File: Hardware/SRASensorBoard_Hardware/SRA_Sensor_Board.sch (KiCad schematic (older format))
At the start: 16 parts

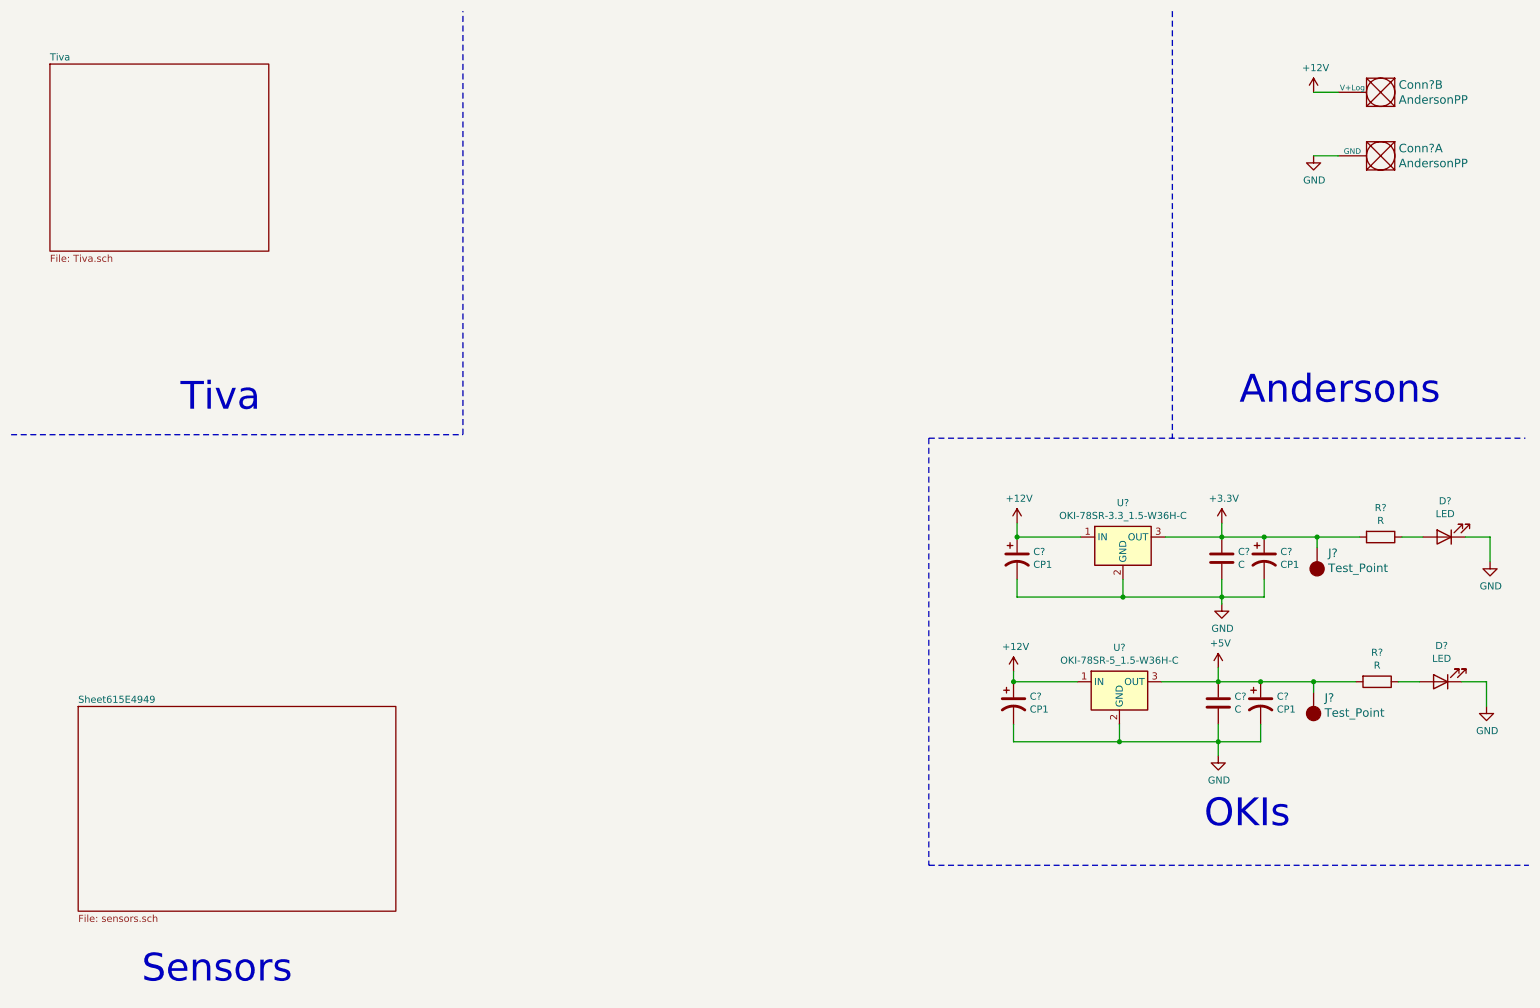
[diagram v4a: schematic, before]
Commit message: Added NH3 sensor and MOSFETS, fixed tiva pins
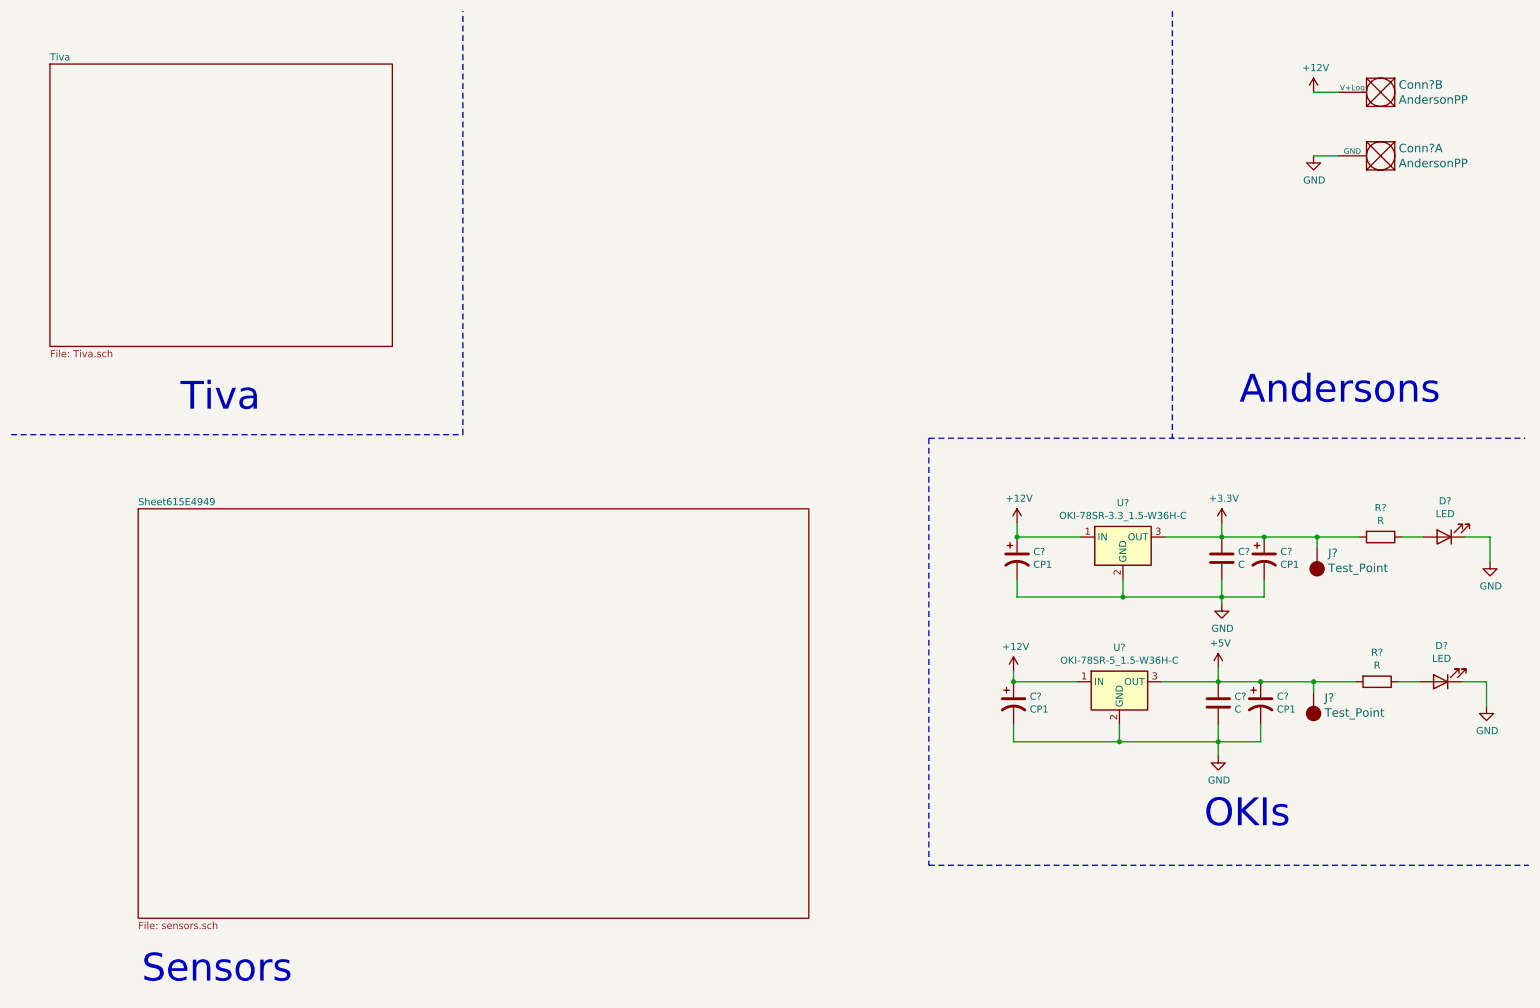
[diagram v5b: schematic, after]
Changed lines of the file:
@@
 $EndComp
 $Sheet
-S 750  850  1550 1325
+S 750  850  2425 2000
 U 614D345C
 F0 "Tiva" 50
@@
 	9875 1050 9700 1050
 $Sheet
-S 950  5400 2250 1450
+S 1375 4000 4750 2900
 U 615E494A
 F0 "Sheet615E4949" 50

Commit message: schematic review meeting
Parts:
- removed C? (x2): CP1, symbol Device:CP1
- removed J? (x2): Test_Point, symbol MRDT_Connectors:Test_Point
- C1, C2: renamed from C?; value CP1 -> 10uf
- C3, C4: renamed from C?; value C -> 10uf
- R1: renamed from R?; value R -> 100
- R2: renamed from R?; value R -> 43
- gave numbers to parts that had none: 5
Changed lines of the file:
@@
 $EndDescr
 $Comp
-L MRDT_Connectors:AndersonPP Conn?
+L MRDT_Connectors:AndersonPP Conn1
 U 2 1 614D19B3
 P 10275 950
-F 0 "Conn?" H 10247 997 60  0000 R CNN
+F 0 "Conn1" H 10247 997 60  0000 R CNN
 F 1 "AndersonPP" H 10247 1103 60  0000 R CNN
 F 2 "" H 10125 400 60  0001 C CNN
@@
 $EndComp
 $Comp
-L MRDT_Connectors:AndersonPP Conn?
+L MRDT_Connectors:AndersonPP Conn1
 U 1 1 614D22E6
 P 10275 1400
-F 0 "Conn?" H 10247 1447 60  0000 R CNN
+F 0 "Conn1" H 10247 1447 60  0000 R CNN
 F 1 "AndersonPP" H 10247 1553 60  0000 R CNN
 F 2 "" H 10125 850 60  0001 C CNN
@@
 	6975 3500 11200 3500
 $Comp
-L Converter_DCDC:OKI-78SR-5_1.5-W36H-C U?
+L Converter_DCDC:OKI-78SR-5_1.5-W36H-C U1
 U 1 1 615099E1
 P 8325 5225
-F 0 "U?" H 8325 5467 50  0000 C CNN
+F 0 "U1" H 8325 5467 50  0000 C CNN
 F 1 "OKI-78SR-5_1.5-W36H-C" H 8325 5376 50  0000 C CNN
 F 2 "Converter_DCDC:Converter_DCDC_muRata_OKI-78SR_Horizontal" H 8375 4975 50  0001 L CIN
@@
 $EndComp
 $Comp
-L Converter_DCDC:OKI-78SR-3.3_1.5-W36H-C U?
+L Converter_DCDC:OKI-78SR-3.3_1.5-W36H-C U2
 U 1 1 61509405
 P 8350 4200
-F 0 "U?" H 8350 4442 50  0000 C CNN
+F 0 "U2" H 8350 4442 50  0000 C CNN
 F 1 "OKI-78SR-3.3_1.5-W36H-C" H 8350 4351 50  0000 C CNN
 F 2 "Converter_DCDC:Converter_DCDC_muRata_OKI-78SR_Horizontal" H 8400 3950 50  0001 L CIN
@@
 $EndComp
 $Comp
-L Device:CP1 C?
+L Device:CP1 C2
 U 1 1 615E1386
 P 7600 4350
-F 0 "C?" H 7715 4396 50  0000 L CNN
-F 1 "CP1" H 7715 4305 50  0000 L CNN
+F 0 "C2" H 7715 4396 50  0000 L CNN
+F 1 "10uf" H 7715 4305 50  0000 L CNN
 F 2 "" H 7600 4350 50  0001 C CNN
 F 3 "~" H 7600 4350 50  0001 C CNN
@@
 $EndComp
 $Comp
-L Device:C C?
+L Device:C C4
 U 1 1 615E2024
 P 9050 4350
-F 0 "C?" H 9165 4396 50  0000 L CNN
-F 1 "C" H 9165 4305 50  0000 L CNN
+F 0 "C4" H 9165 4396 50  0000 L CNN
+F 1 "10uf" H 9165 4305 50  0000 L CNN
 F 2 "" H 9088 4200 50  0001 C CNN
 F 3 "~" H 9050 4350 50  0001 C CNN
@@
 $EndComp
 $Comp
-L Device:CP1 C?
-U 1 1 615E2538
-P 9350 4350
-F 0 "C?" H 9465 4396 50  0000 L CNN
-F 1 "CP1" H 9465 4305 50  0000 L CNN
-F 2 "" H 9350 4350 50  0001 C CNN
-F 3 "~" H 9350 4350 50  0001 C CNN
-	1    9350 4350
-	1    0    0    -1
-$EndComp
-$Comp
-L MRDT_Connectors:Test_Point J?
-U 1 1 615E33B2
-P 9725 4275
-F 0 "J?" H 9647 4314 60  0000 R CNN
-F 1 "Test_Point" H 9647 4420 60  0000 R CNN
-F 2 "" H 9725 4225 60  0001 C CNN
-F 3 "" H 9725 4225 60  0001 C CNN
-	1    9725 4275
-	-1   0    0    1
-$EndComp
-$Comp
-L Device:R R?
+L Device:R R2
 U 1 1 615E4C25
 P 10175 4200
-F 0 "R?" V 9968 4200 50  0000 C CNN
-F 1 "R" V 10059 4200 50  0000 C CNN
+F 0 "R2" V 9968 4200 50  0000 C CNN
+F 1 "43" V 10059 4200 50  0000 C CNN
 F 2 "" V 10105 4200 50  0001 C CNN
 F 3 "~" H 10175 4200 50  0001 C CNN
@@
 $EndComp
 $Comp
-L Device:LED D?
+L Device:LED D2
 U 1 1 615E5345
 P 10625 4200
-F 0 "D?" H 10618 3945 50  0000 C CNN
+F 0 "D2" H 10618 3945 50  0000 C CNN
 F 1 "LED" H 10618 4036 50  0000 C CNN
 F 2 "" H 10625 4200 50  0001 C CNN
@@
 $EndComp
 $Comp
-L power:GND #PWR?
+L power:GND #PWR0101
 U 1 1 615E5F0A
 P 10950 4375
-F 0 "#PWR?" H 10950 4125 50  0001 C CNN
+F 0 "#PWR0101" H 10950 4125 50  0001 C CNN
 F 1 "GND" H 10955 4202 50  0000 C CNN
 F 2 "" H 10950 4375 50  0001 C CNN
@@
 	8350 4625 9050 4625
 Connection ~ 8350 4625
-Wire Wire Line
-	9050 4625 9350 4625
-Wire Wire Line
-	9350 4625 9350 4500
 Connection ~ 9050 4625
-Wire Wire Line
-	9350 4200 9050 4200
 Connection ~ 9050 4200
 Wire Wire Line
-	9350 4200 9725 4200
-Wire Wire Line
-	9725 4200 9725 4275
-Connection ~ 9350 4200
-Connection ~ 9725 4200
-Wire Wire Line
 	10325 4200 10475 4200
 Wire Wire Line
@@
 Wire Wire Line
 	8650 4200 9050 4200
-Wire Wire Line
-	9725 4200 10025 4200
-$Comp
-L Device:CP1 C?
+$Comp
+L Device:CP1 C1
 U 1 1 615EE19D
 P 7575 5375
-F 0 "C?" H 7690 5421 50  0000 L CNN
-F 1 "CP1" H 7690 5330 50  0000 L CNN
+F 0 "C1" H 7690 5421 50  0000 L CNN
+F 1 "10uf" H 7690 5330 50  0000 L CNN
 F 2 "" H 7575 5375 50  0001 C CNN
 F 3 "~" H 7575 5375 50  0001 C CNN
@@
 $EndComp
 $Comp
-L Device:C C?
+L Device:C C3
 U 1 1 615EE1A3
 P 9025 5375
-F 0 "C?" H 9140 5421 50  0000 L CNN
-F 1 "C" H 9140 5330 50  0000 L CNN
+F 0 "C3" H 9140 5421 50  0000 L CNN
+F 1 "10uf" H 9140 5330 50  0000 L CNN
 F 2 "" H 9063 5225 50  0001 C CNN
 F 3 "~" H 9025 5375 50  0001 C CNN
@@
 $EndComp
 $Comp
-L Device:CP1 C?
-U 1 1 615EE1A9
-P 9325 5375
-F 0 "C?" H 9440 5421 50  0000 L CNN
-F 1 "CP1" H 9440 5330 50  0000 L CNN
-F 2 "" H 9325 5375 50  0001 C CNN
-F 3 "~" H 9325 5375 50  0001 C CNN
-	1    9325 5375
-	1    0    0    -1
-$EndComp
-$Comp
-L MRDT_Connectors:Test_Point J?
-U 1 1 615EE1AF
-P 9700 5300
-F 0 "J?" H 9622 5339 60  0000 R CNN
-F 1 "Test_Point" H 9622 5445 60  0000 R CNN
-F 2 "" H 9700 5250 60  0001 C CNN
-F 3 "" H 9700 5250 60  0001 C CNN
-	1    9700 5300
-	-1   0    0    1
-$EndComp
-$Comp
-L Device:R R?
+L Device:R R1
 U 1 1 615EE1B5
 P 10150 5225
-F 0 "R?" V 9943 5225 50  0000 C CNN
-F 1 "R" V 10034 5225 50  0000 C CNN
+F 0 "R1" V 9943 5225 50  0000 C CNN
+F 1 "100" V 10034 5225 50  0000 C CNN
 F 2 "" V 10080 5225 50  0001 C CNN
 F 3 "~" H 10150 5225 50  0001 C CNN
@@
 $EndComp
 $Comp
-L Device:LED D?
+L Device:LED D1
 U 1 1 615EE1BB
 P 10600 5225
-F 0 "D?" H 10593 4970 50  0000 C CNN
+F 0 "D1" H 10593 4970 50  0000 C CNN
 F 1 "LED" H 10593 5061 50  0000 C CNN
 F 2 "" H 10600 5225 50  0001 C CNN
@@
 $EndComp
 $Comp
-L power:GND #PWR?
+L power:GND #PWR0102
 U 1 1 615EE1C1
 P 10925 5400
-F 0 "#PWR?" H 10925 5150 50  0001 C CNN
+F 0 "#PWR0102" H 10925 5150 50  0001 C CNN
 F 1 "GND" H 10930 5227 50  0000 C CNN
 F 2 "" H 10925 5400 50  0001 C CNN
@@
 	8325 5650 9025 5650
 Connection ~ 8325 5650
-Wire Wire Line
-	9025 5650 9325 5650
-Wire Wire Line
-	9325 5650 9325 5525
 Connection ~ 9025 5650
-Wire Wire Line
-	9325 5225 9025 5225
 Connection ~ 9025 5225
 Wire Wire Line
-	9325 5225 9700 5225
-Wire Wire Line
-	9700 5225 9700 5300
-Connection ~ 9325 5225
-Connection ~ 9700 5225
-Wire Wire Line
 	10300 5225 10450 5225
 Wire Wire Line
@@
 Wire Wire Line
 	8625 5225 9025 5225
-Wire Wire Line
-	9700 5225 10000 5225
-$Comp
-L power:+12V #PWR?
+$Comp
+L power:+12V #PWR0103
 U 1 1 615F977E
 P 9700 1050
-F 0 "#PWR?" H 9700 900 50  0001 C CNN
+F 0 "#PWR0103" H 9700 900 50  0001 C CNN
 F 1 "+12V" H 9715 1223 50  0000 C CNN
 F 2 "" H 9700 1050 50  0001 C CNN
@@
 $EndComp
 $Comp
-L power:GND #PWR?
+L power:GND #PWR0104
 U 1 1 615FA471
 P 9700 1500
-F 0 "#PWR?" H 9700 1250 50  0001 C CNN
+F 0 "#PWR0104" H 9700 1250 50  0001 C CNN
 F 1 "GND" H 9705 1327 50  0000 C CNN
 F 2 "" H 9700 1500 50  0001 C CNN
@@
 $EndSheet
 $Comp
-L power:+12V #PWR?
+L power:+12V #PWR0105
 U 1 1 615EE1DD
 P 7600 4100
-F 0 "#PWR?" H 7600 3950 50  0001 C CNN
+F 0 "#PWR0105" H 7600 3950 50  0001 C CNN
 F 1 "+12V" H 7615 4273 50  0000 C CNN
 F 2 "" H 7600 4100 50  0001 C CNN
@@
 $EndComp
 $Comp
-L power:+12V #PWR?
+L power:+12V #PWR0106
 U 1 1 615EEAA7
 P 7575 5150
-F 0 "#PWR?" H 7575 5000 50  0001 C CNN
+F 0 "#PWR0106" H 7575 5000 50  0001 C CNN
 F 1 "+12V" H 7590 5323 50  0000 C CNN
 F 2 "" H 7575 5150 50  0001 C CNN
@@
 Connection ~ 7600 4200
 $Comp
-L power:+5V #PWR?
+L power:+5V #PWR0107
 U 1 1 615F1C53
 P 9025 5125
-F 0 "#PWR?" H 9025 4975 50  0001 C CNN
+F 0 "#PWR0107" H 9025 4975 50  0001 C CNN
 F 1 "+5V" H 9040 5298 50  0000 C CNN
 F 2 "" H 9025 5125 50  0001 C CNN
@@
 	9025 5225 9025 5125
 $Comp
-L power:+3.3V #PWR?
+L power:+3.3V #PWR0108
 U 1 1 615F3DA4
 P 9050 4100
-F 0 "#PWR?" H 9050 3950 50  0001 C CNN
+F 0 "#PWR0108" H 9050 3950 50  0001 C CNN
 F 1 "+3.3V" H 9065 4273 50  0000 C CNN
 F 2 "" H 9050 4100 50  0001 C CNN
@@
 	9050 4200 9050 4100
 $Comp
-L power:GND #PWR?
+L power:GND #PWR0109
 U 1 1 615F5CA8
 P 9025 5750
-F 0 "#PWR?" H 9025 5500 50  0001 C CNN
+F 0 "#PWR0109" H 9025 5500 50  0001 C CNN
 F 1 "GND" H 9030 5577 50  0000 C CNN
 F 2 "" H 9025 5750 50  0001 C CNN
@@
 	9025 5750 9025 5650
 $Comp
-L power:GND #PWR?
+L power:GND #PWR0110
 U 1 1 615F72EB
 P 9050 4675
-F 0 "#PWR?" H 9050 4425 50  0001 C CNN
+F 0 "#PWR0110" H 9050 4425 50  0001 C CNN
 F 1 "GND" H 9055 4502 50  0000 C CNN
 F 2 "" H 9050 4675 50  0001 C CNN
@@
 Wire Wire Line
 	9050 4675 9050 4625
+Wire Wire Line
+	9025 5225 10000 5225
+Wire Wire Line
+	9050 4200 10025 4200
 $EndSCHEMATC

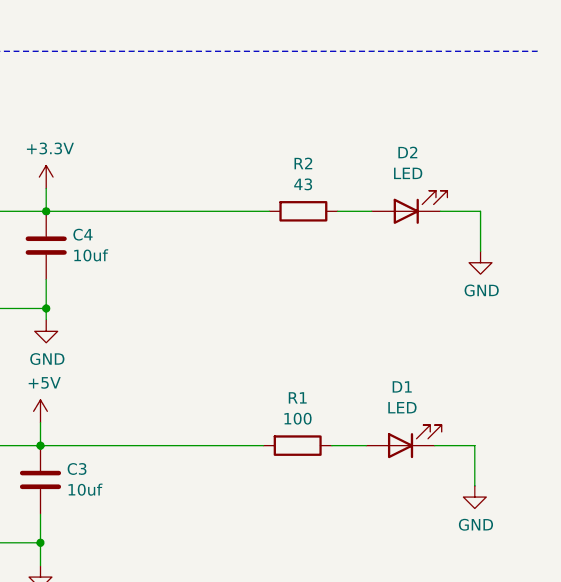
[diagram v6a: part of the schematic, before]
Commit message: Labeled LED Colors
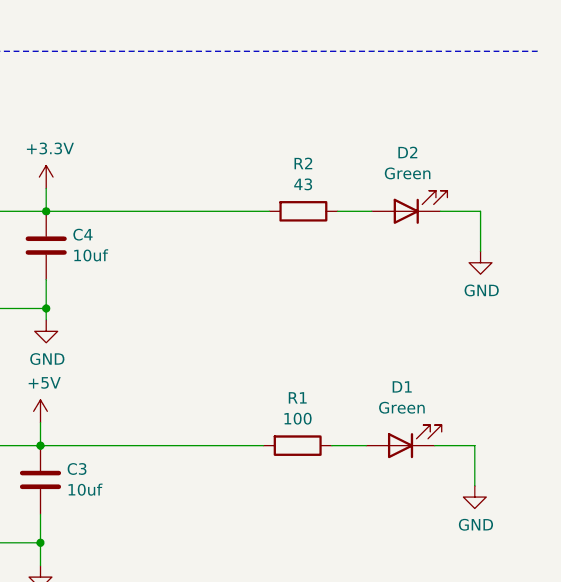
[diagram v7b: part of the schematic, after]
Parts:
- D1, D2: value LED -> Green
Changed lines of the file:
@@
 P 10625 4200
 F 0 "D2" H 10618 3945 50  0000 C CNN
-F 1 "LED" H 10618 4036 50  0000 C CNN
+F 1 "Green" H 10618 4036 50  0000 C CNN
 F 2 "" H 10625 4200 50  0001 C CNN
 F 3 "~" H 10625 4200 50  0001 C CNN
@@
 P 10600 5225
 F 0 "D1" H 10593 4970 50  0000 C CNN
-F 1 "LED" H 10593 5061 50  0000 C CNN
+F 1 "Green" H 10593 5061 50  0000 C CNN
 F 2 "" H 10600 5225 50  0001 C CNN
 F 3 "~" H 10600 5225 50  0001 C CNN

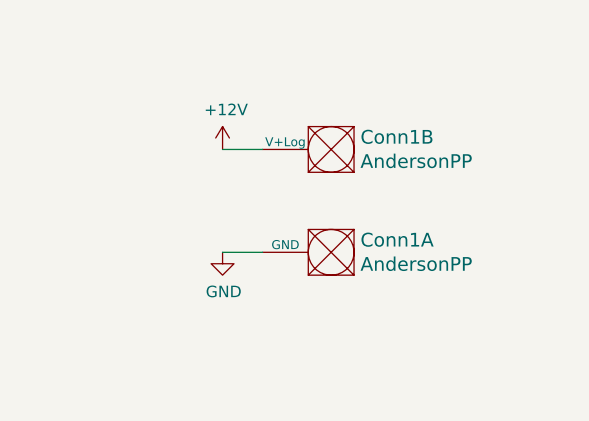
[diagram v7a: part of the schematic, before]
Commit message: Footprint, Layout started
Replaced each 480 ohm resistor with 2 240 ohm resistors b/c we could not find 480 in stock. Footprints for board filled out. Organized components that need to be connected near each other, board placement and wires still need to be done. Board outline created.
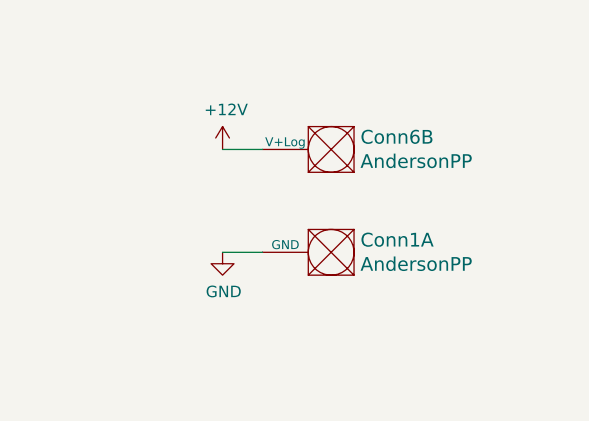
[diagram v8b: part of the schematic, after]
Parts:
- C1, C2, C3, C4: footprint (none) -> Capacitor_SMD:C_0603_1608Metric_Pad1.05x0.95mm_HandSolder
- Conn1: footprint (none) -> MRDT_Connectors:Anderson_1_Horizontal
- Conn6: renamed from Conn1; footprint (none) -> MRDT_Connectors:Anderson_1_Horizontal
- D1, D2: footprint (none) -> LED_SMD:LED_0603_1608Metric_Pad1.05x0.95mm_HandSolder
- R1: footprint (none) -> Resistor_SMD:R_0402_1005Metric
- R2: footprint (none) -> Resistor_SMD:R_0603_1608Metric_Pad1.05x0.95mm_HandSolder
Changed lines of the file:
@@
 $EndDescr
 $Comp
-L MRDT_Connectors:AndersonPP Conn1
+L MRDT_Connectors:AndersonPP Conn6
 U 2 1 614D19B3
 P 10275 950
-F 0 "Conn1" H 10247 997 60  0000 R CNN
+F 0 "Conn6" H 10247 997 60  0000 R CNN
 F 1 "AndersonPP" H 10247 1103 60  0000 R CNN
-F 2 "" H 10125 400 60  0001 C CNN
+F 2 "MRDT_Connectors:Anderson_1_Horizontal" H 10125 400 60  0001 C CNN
 F 3 "" H 10125 400 60  0001 C CNN
 	2    10275 950
@@
 F 0 "Conn1" H 10247 1447 60  0000 R CNN
 F 1 "AndersonPP" H 10247 1553 60  0000 R CNN
-F 2 "" H 10125 850 60  0001 C CNN
+F 2 "MRDT_Connectors:Anderson_1_Horizontal" H 10125 850 60  0001 C CNN
 F 3 "" H 10125 850 60  0001 C CNN
 	1    10275 1400
@@
 F 0 "C2" H 7715 4396 50  0000 L CNN
 F 1 "10uf" H 7715 4305 50  0000 L CNN
-F 2 "" H 7600 4350 50  0001 C CNN
+F 2 "Capacitor_SMD:C_0603_1608Metric_Pad1.05x0.95mm_HandSolder" H 7600 4350 50  0001 C CNN
 F 3 "~" H 7600 4350 50  0001 C CNN
 	1    7600 4350
@@
 F 0 "C4" H 9165 4396 50  0000 L CNN
 F 1 "10uf" H 9165 4305 50  0000 L CNN
-F 2 "" H 9088 4200 50  0001 C CNN
+F 2 "Capacitor_SMD:C_0603_1608Metric_Pad1.05x0.95mm_HandSolder" H 9088 4200 50  0001 C CNN
 F 3 "~" H 9050 4350 50  0001 C CNN
 	1    9050 4350
@@
 F 0 "R2" V 9968 4200 50  0000 C CNN
 F 1 "43" V 10059 4200 50  0000 C CNN
-F 2 "" V 10105 4200 50  0001 C CNN
+F 2 "Resistor_SMD:R_0603_1608Metric_Pad1.05x0.95mm_HandSolder" V 10105 4200 50  0001 C CNN
 F 3 "~" H 10175 4200 50  0001 C CNN
 	1    10175 4200
@@
 F 0 "D2" H 10618 3945 50  0000 C CNN
 F 1 "Green" H 10618 4036 50  0000 C CNN
-F 2 "" H 10625 4200 50  0001 C CNN
+F 2 "LED_SMD:LED_0603_1608Metric_Pad1.05x0.95mm_HandSolder" H 10625 4200 50  0001 C CNN
 F 3 "~" H 10625 4200 50  0001 C CNN
 	1    10625 4200
@@
 F 0 "C1" H 7690 5421 50  0000 L CNN
 F 1 "10uf" H 7690 5330 50  0000 L CNN
-F 2 "" H 7575 5375 50  0001 C CNN
+F 2 "Capacitor_SMD:C_0603_1608Metric_Pad1.05x0.95mm_HandSolder" H 7575 5375 50  0001 C CNN
 F 3 "~" H 7575 5375 50  0001 C CNN
 	1    7575 5375
@@
 F 0 "C3" H 9140 5421 50  0000 L CNN
 F 1 "10uf" H 9140 5330 50  0000 L CNN
-F 2 "" H 9063 5225 50  0001 C CNN
+F 2 "Capacitor_SMD:C_0603_1608Metric_Pad1.05x0.95mm_HandSolder" H 9063 5225 50  0001 C CNN
 F 3 "~" H 9025 5375 50  0001 C CNN
 	1    9025 5375
@@
 F 0 "R1" V 9943 5225 50  0000 C CNN
 F 1 "100" V 10034 5225 50  0000 C CNN
-F 2 "" V 10080 5225 50  0001 C CNN
+F 2 "Resistor_SMD:R_0402_1005Metric" V 10080 5225 50  0001 C CNN
 F 3 "~" H 10150 5225 50  0001 C CNN
 	1    10150 5225
@@
 F 0 "D1" H 10593 4970 50  0000 C CNN
 F 1 "Green" H 10593 5061 50  0000 C CNN
-F 2 "" H 10600 5225 50  0001 C CNN
+F 2 "LED_SMD:LED_0603_1608Metric_Pad1.05x0.95mm_HandSolder" H 10600 5225 50  0001 C CNN
 F 3 "~" H 10600 5225 50  0001 C CNN
 	1    10600 5225
